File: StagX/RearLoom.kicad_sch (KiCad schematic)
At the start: 3 parts

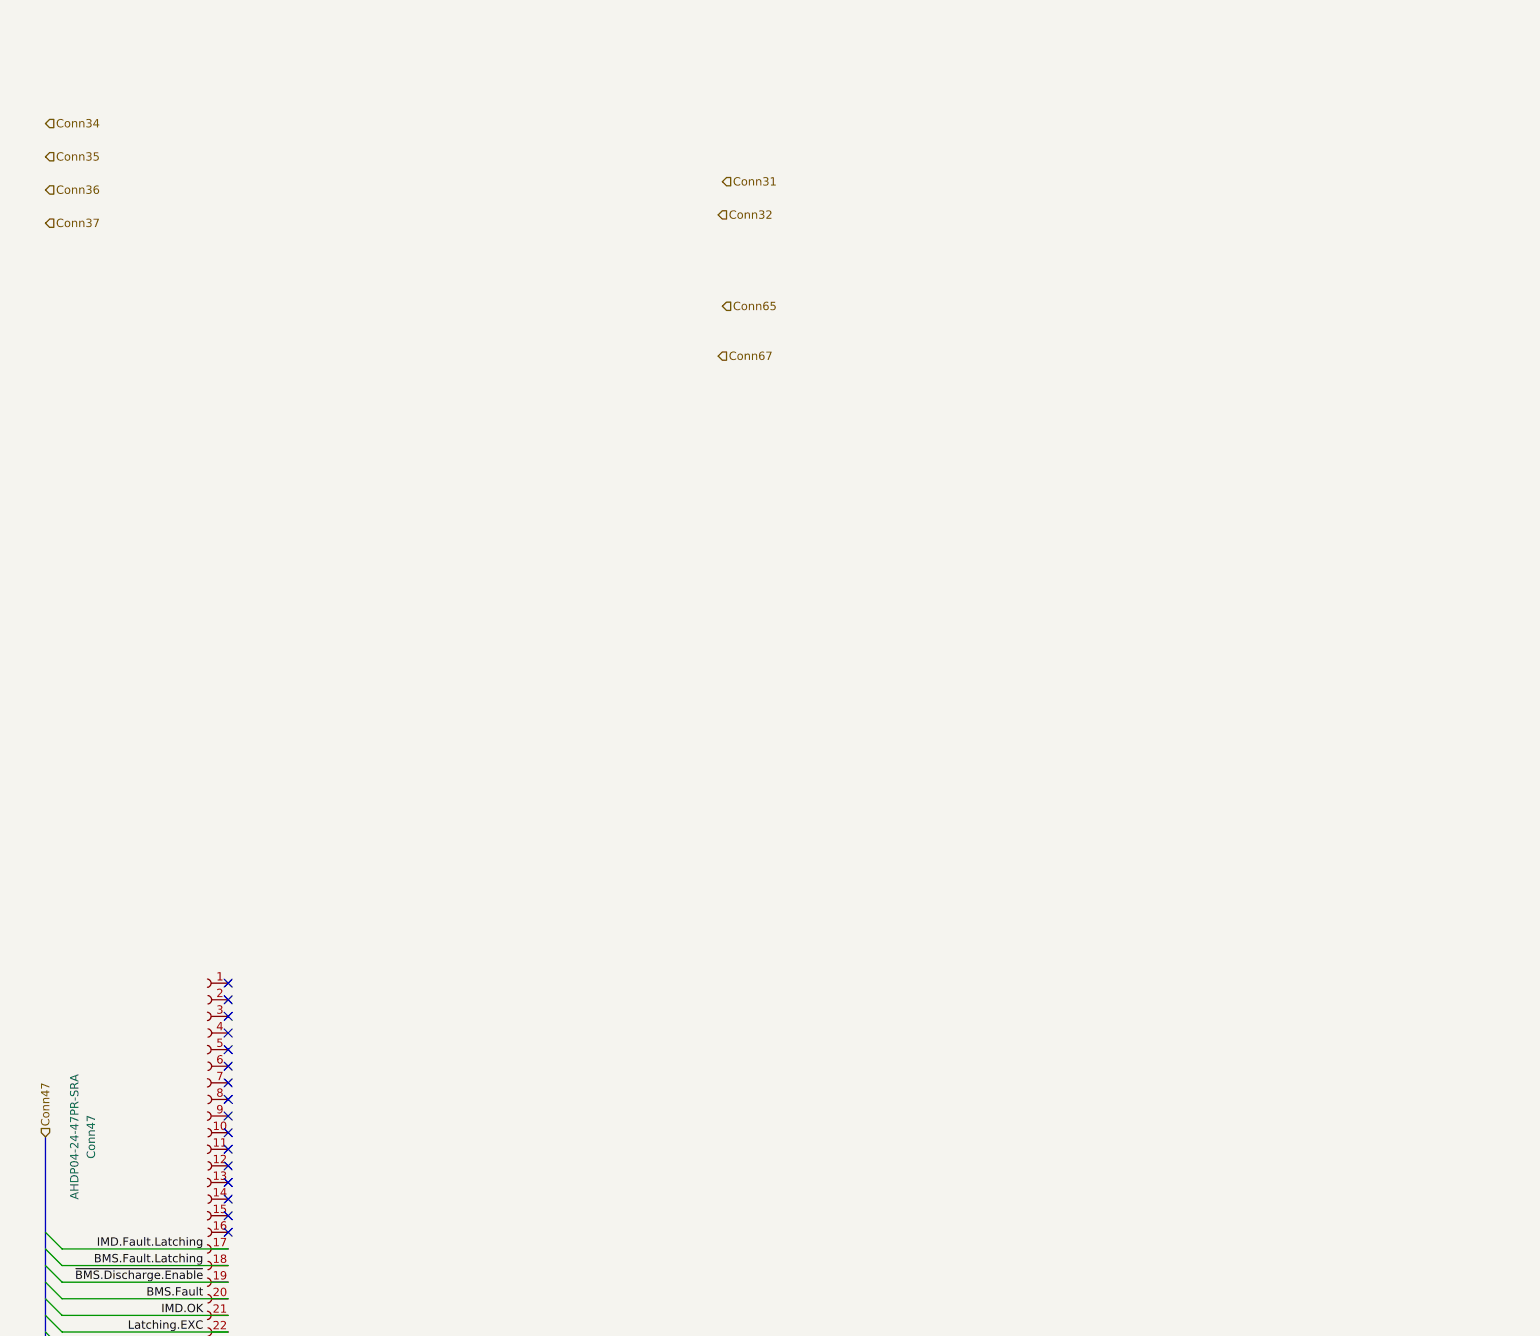
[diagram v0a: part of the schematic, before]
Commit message: feat(RearLoom): completed Inverter, Motor and Resolver sheet
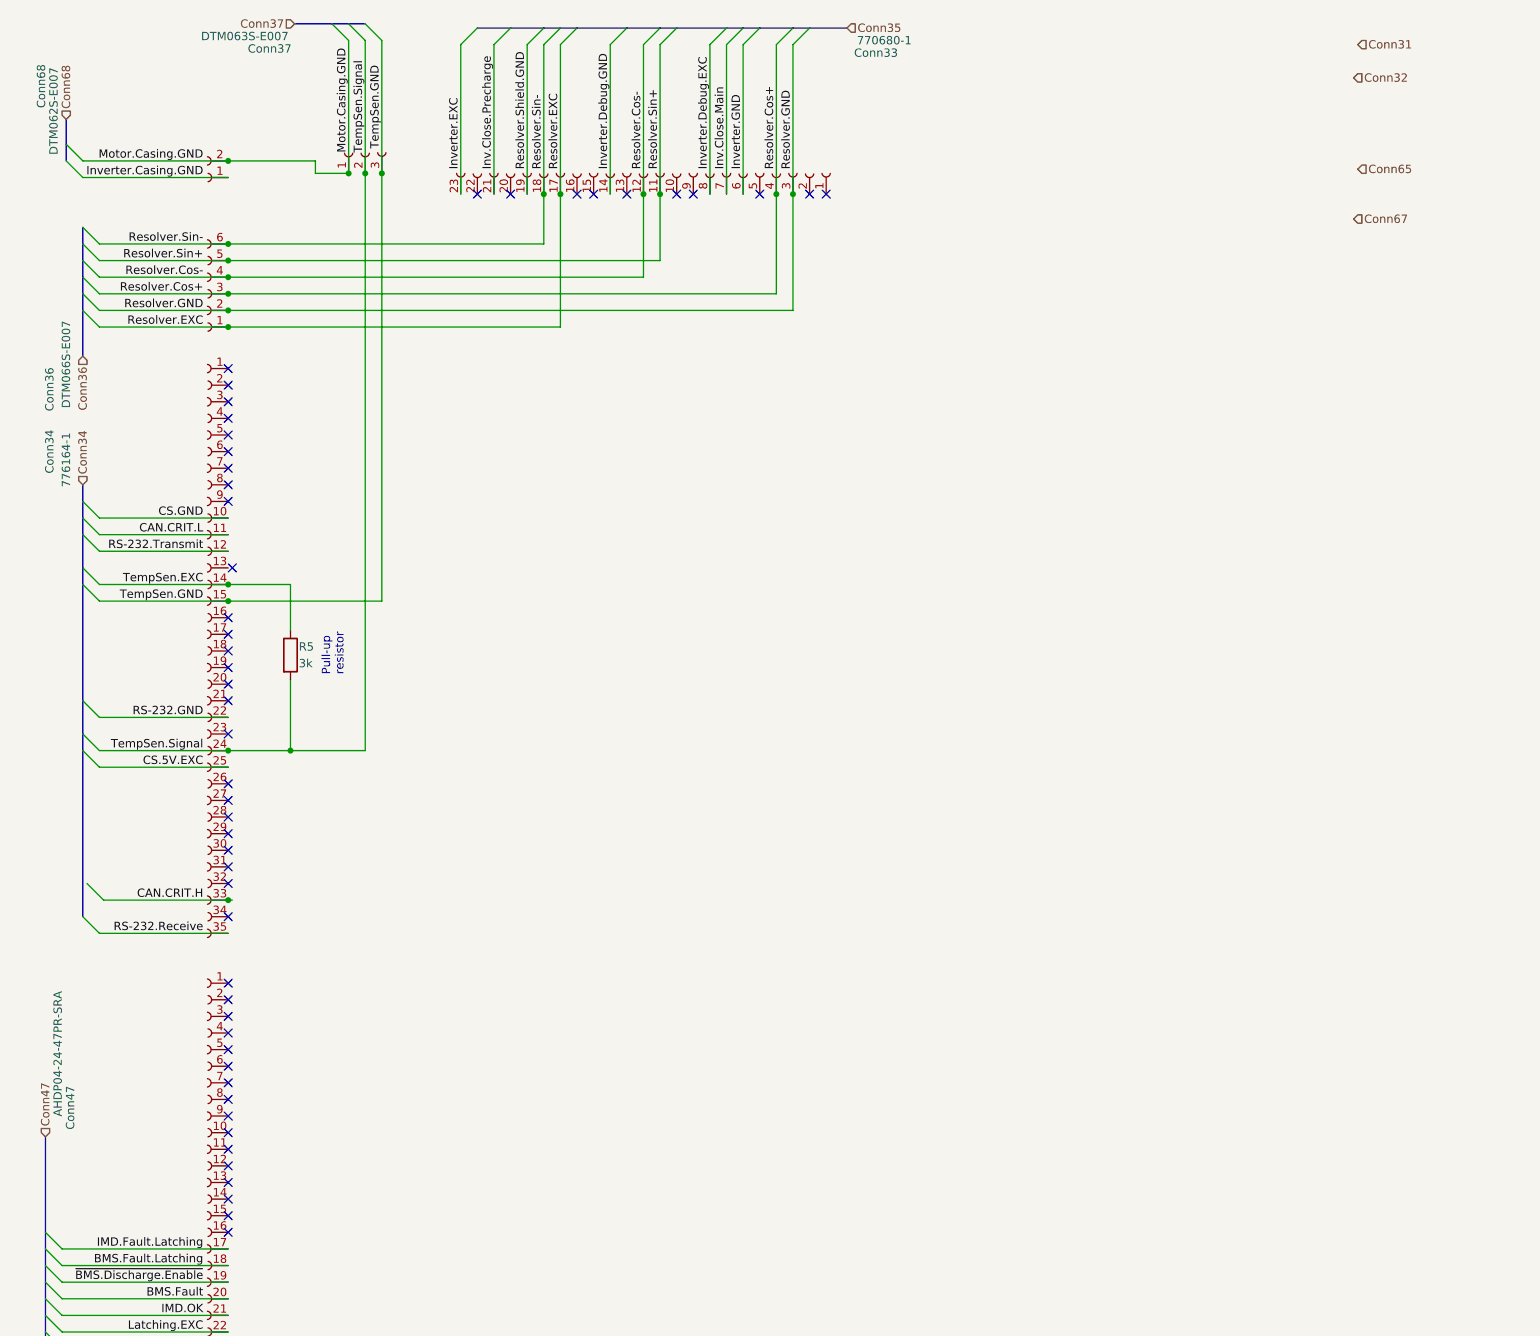
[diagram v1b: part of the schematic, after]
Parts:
- added Conn33: J2 Inverter Connector, symbol Connectors_SUFST:J2 Inverter Connector
- added Conn34: J1 Inverter Connector, symbol Connectors_SUFST:J1 Inverter Connector
- added Conn36: Deutsch_DTM_6S_Pin, symbol Connectors_SUFST:Deutsch_DTM_6S_Pin
- added Conn37: Deutsch_DTM_3S_Pin, symbol Connectors_SUFST:Deutsch_DTM_3S_Pin
- added Conn68: Deutsch_DTM_2S_Pin, symbol Connectors_SUFST:Deutsch_DTM_2S_Pin
- added R5: 3k, symbol Device:R
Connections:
- new net CAN.CRIT.H: Conn34.33
- new net CAN.CRIT.L: Conn34.11
- new net CS.5V.EXC: Conn34.25
- new net CS.GND: Conn34.10
- new net Inv.Close.Main: Conn33.7
- new net Inv.Close.Precharge: Conn33.21
- new net Inverter.Casing.GND: Conn68.1
- new net Inverter.Debug.EXC: Conn33.8
- new net Inverter.Debug.GND: Conn33.14
- new net Inverter.EXC: Conn33.23
- new net Inverter.GND: Conn33.6
- new net Motor.Casing.GND: Conn37.1, Conn68.2
- new net RS-232.GND: Conn34.22
- new net RS-232.Receive: Conn34.35
- new net RS-232.Transmit: Conn34.12
- new net Resolver.Cos+: Conn33.4, Conn36.3
- new net Resolver.Cos-: Conn33.12, Conn36.4
- new net Resolver.EXC: Conn33.17, Conn36.1
- new net Resolver.GND: Conn33.3, Conn36.2
- new net Resolver.Shield.GND: Conn33.19
- new net Resolver.Sin+: Conn33.11, Conn36.5
- new net Resolver.Sin-: Conn33.18, Conn36.6
- new net TempSen.EXC: Conn34.14, R5.1
- new net TempSen.GND: Conn34.15, Conn37.3
- new net TempSen.Signal: Conn34.24, Conn37.2, R5.2
- no-connect marks 36 -> 71
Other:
- note added: "Pull-up resistor"
- company: (none) -> SUFST
- title: (none) -> Rear Loom

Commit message: feat(RearLoom): progress with Rear Loom. Miising Power and GND
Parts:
- added Conn68: Deutsch_DTM_2S_Pin, symbol Connectors_SUFST:Deutsch_DTM_2S_Pin
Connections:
- net HV_Sense.EXC is gone; now on net REB.HVS.BATT.EXC: Conn47.5
- net Inv.Close.Main is gone; now on net INV.Close.+AIR: Conn33.7
- net Inv.Close.Precharge is gone; now on net INV.Close.PCHG: Conn33.21
- net ~{BMS.Fault} is gone; now on net BMS.Fault: Conn47.29
- net -AIR.GND: now also Conn47.42, Conn47.43
- net REB.HVS.BATT.GND: now also Conn47.14
- net SHUT.TSAC.Interlock: now also Conn68.2
- net ~{TS.Detected}: now also Conn47.26
- net SHUT.IN renamed SHUT.TRC
- net SHUT.TRC: now also Conn68.1
- removed net TS.Detected: Conn47.14, Conn47.26
- no-connect marks 71 -> 69

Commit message: feat(RearLoom): PWR and GND complete. progress on top-level
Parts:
- added Conn31: Conn A PDM Connector, symbol Connectors_SUFST:Conn A PDM Connector
- added Conn32: Conn C PDM Connector, symbol Connectors_SUFST:Conn C PDM Connector
- added Conn65: Ring Terminals, symbol Connector:Conn_01x16_Socket
- added Conn73, Conn74: Deutsch_DTM_2S_Pin, symbol Connectors_SUFST:Deutsch_DTM_2S_Pin
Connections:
- net Chassis.GND is gone; now on net Conn67: Conn47.8
- net -AIR.GND: no longer Conn47.42
- net Accumulator.GND: now also Conn65.1 (Pin_1)
- net Accumulator.GND.2: now also Conn65.2 (Pin_2)
- net BMS.EXC: now also Conn31.2
- net CAN.S.HIGH: now also Conn31.10
- net CAN.S.LOW: now also Conn31.9
- net IMD.EXC: now also Conn31.1
- net Inverter.Casing.GND: now also Conn65.5 (Pin_5)
- net Inverter.EXC: now also Conn31.11
- net Inverter.GND: now also Conn65.3 (Pin_3)
- net Isolator.EXC: now also Conn31.3
- net Latching.EXC: now also Conn31.12
- net Latching.GND: now also Conn65.6 (Pin_6)
- net SidePannel.GND: now also Conn65.4 (Pin_4)
- net TSAL.EXC: now also Conn31.13
- net TSAL.GND: now also Conn65.7 (Pin_7)
- net Resolver.Shield.GND: no longer names the net of Conn33.19
- new net Brake.Light.EXC: Conn32.2
- new net Dashbox.EXC: Conn32.3
- new net Fan.EXC: Conn32.1
- new net PDM.GND.1: Conn31.26, Conn65.12 (Pin_12)
- new net PDM.GND.2: Conn31.25, Conn65.11 (Pin_11)
- new net Pedalbox.EXC: Conn32.4
- new net Pump1.EXC: Conn31.14, Conn73.1
- new net Pump1.GND: Conn65.9 (Pin_9), Conn73.2
- new net Pump2.EXC: Conn31.15, Conn74.1
- new net Pump2.GND: Conn65.10 (Pin_10), Conn74.2
- new net SHUT.GND: Conn47.42, Conn65.8 (Pin_8)
- no-connect marks 69 -> 88
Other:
- note added: "RS232.EXC missing?"
- moved on the sheet: Conn47, Conn68

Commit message: feat(RearLoom): Rear Loom Completed
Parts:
- added Conn72: Current Sensor Connector, symbol Connectors_SUFST:Current Sensor Connector
- added Conn75: AMPHENOL-47P-Recepticle, symbol Connectors_SUFST:AMPHENOL-47P-Recepticle
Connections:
- net BMS.Fault.Latching: now also Conn75.8
- net Brake.Light.EXC: now also Conn75.4
- net CAN.S.HIGH: now also Conn75.16
- net CAN.S.LOW: now also Conn75.15
- net CS.5V.EXC: now also Conn72.1
- net CS.GND: now also Conn72.3
- net Cockpit.Red.LED.GND: now also Conn75.11
- net Dashbox.EXC: now also Conn75.5
- net Fan.EXC: now also Conn75.3
- net IMD.Fault.Latching: now also Conn75.7
- net Pedalbox.EXC: now also Conn75.6
- net RS-232.GND: now also Conn75.21
- net RS-232.Receive: now also Conn75.20
- net RS-232.Transmit: now also Conn75.19
- net SHUT.HVD.Interlock: now also Conn75.9
- net SHUT.Right.E-Stop: now also Conn75.10
- net TS.ON: now also Conn75.2
- net TS.Ready: now also Conn75.1
- net TSAL.Green.LED.GND: now also Conn75.13
- net TSAL.LED.EXC: now also Conn75.14
- net TSAL.Red.LED.GND: now also Conn75.12
- net Dashbox.GND: now reaches Conn65.13 (Pin_13)
- net Dashbox.GND: now also Conn75.22
- net Pedalbox.GND: now reaches Conn65.14 (Pin_14)
- net Pedalbox.GND: now also Conn75.23
- net CAN.CRIT.H renamed CAN.C.HIGH
- net CAN.C.HIGH: now also Conn75.18
- net CAN.CRIT.L renamed CAN.C.LOW
- net CAN.C.LOW: now also Conn75.17
- net Inverter.Debug.EXC: no longer names the net of Conn33.8
- net Inverter.Debug.GND: no longer names the net of Conn33.14
- new net CT.SIG: Conn72.2, Conn75.24
- no-connect marks 88 -> 90
